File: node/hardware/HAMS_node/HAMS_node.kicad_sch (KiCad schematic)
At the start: 45 parts, among them J1 Conn_01x02, J2 Conn_02x07_Odd_Even, J3 Conn_01x04, J4 Conn_01x04, J5 Conn_01x04, J6 Conn_01x04, J7 Conn_01x08, Q1 DMP3099L, SW1 TL3305BF100QG, SW2 TL3305BF100QG, U1 STM32L031K6Tx, U2 NRF24L01_Breakout, U3 nRF24L01p SMD module, Y1 CM9V-T1A

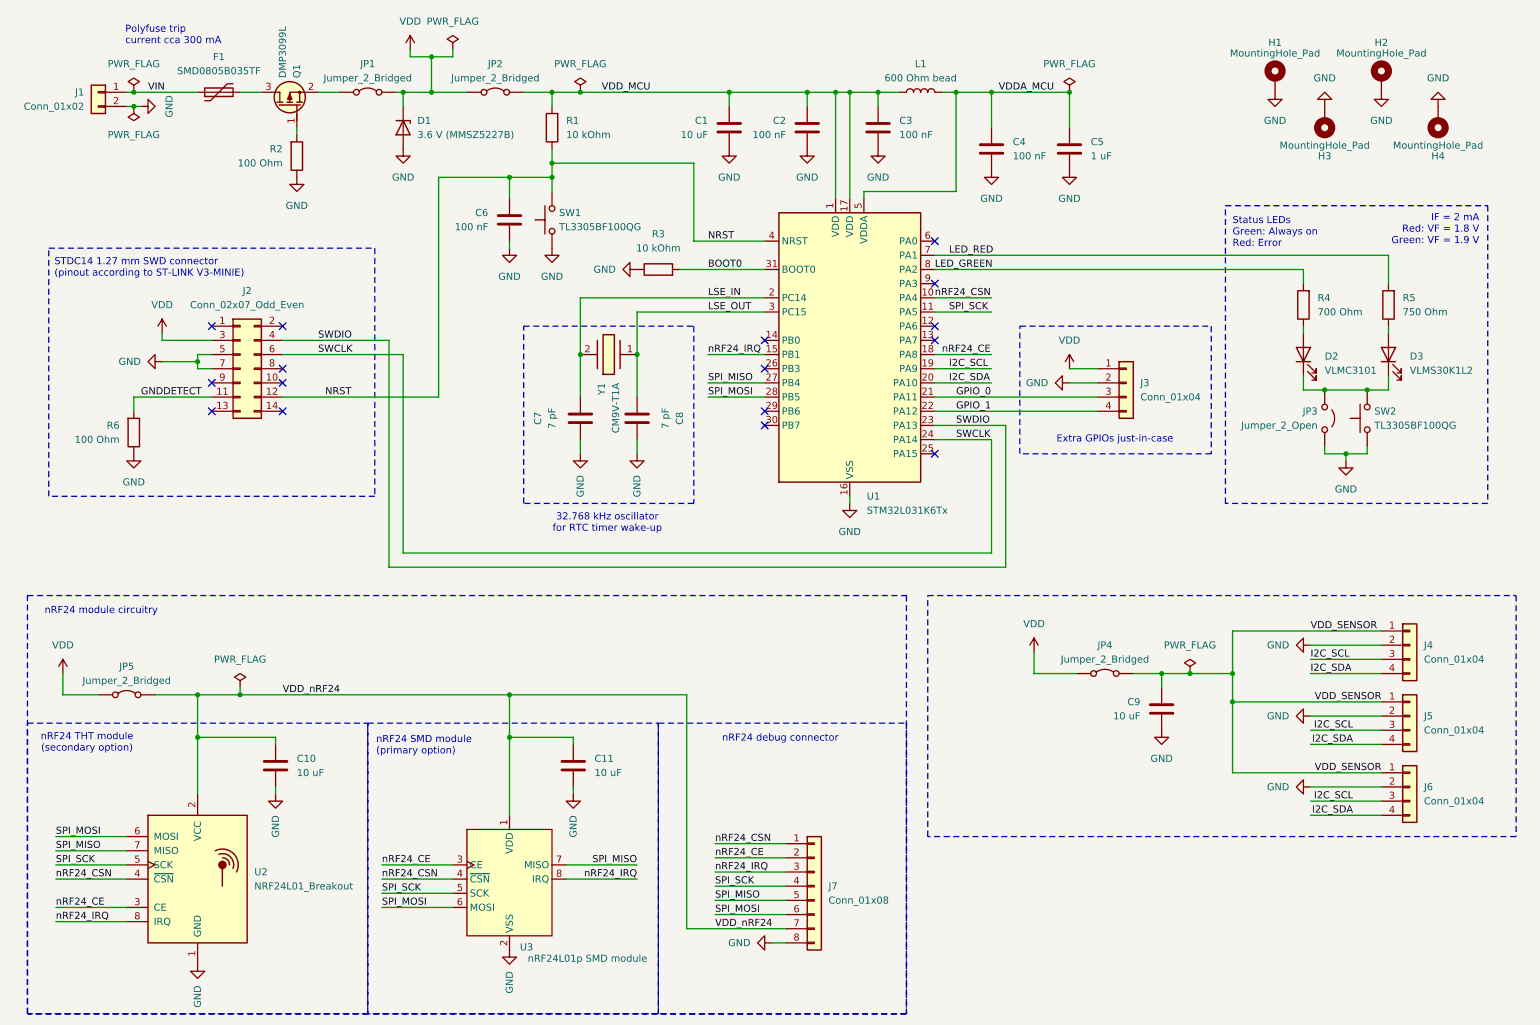
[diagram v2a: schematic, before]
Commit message: Improve HAMS node HW: PCB resize, optimization
Optimize MCU pinout with respect to PCB routing.
Change PCB size to 47.5 mm x 50 mm.
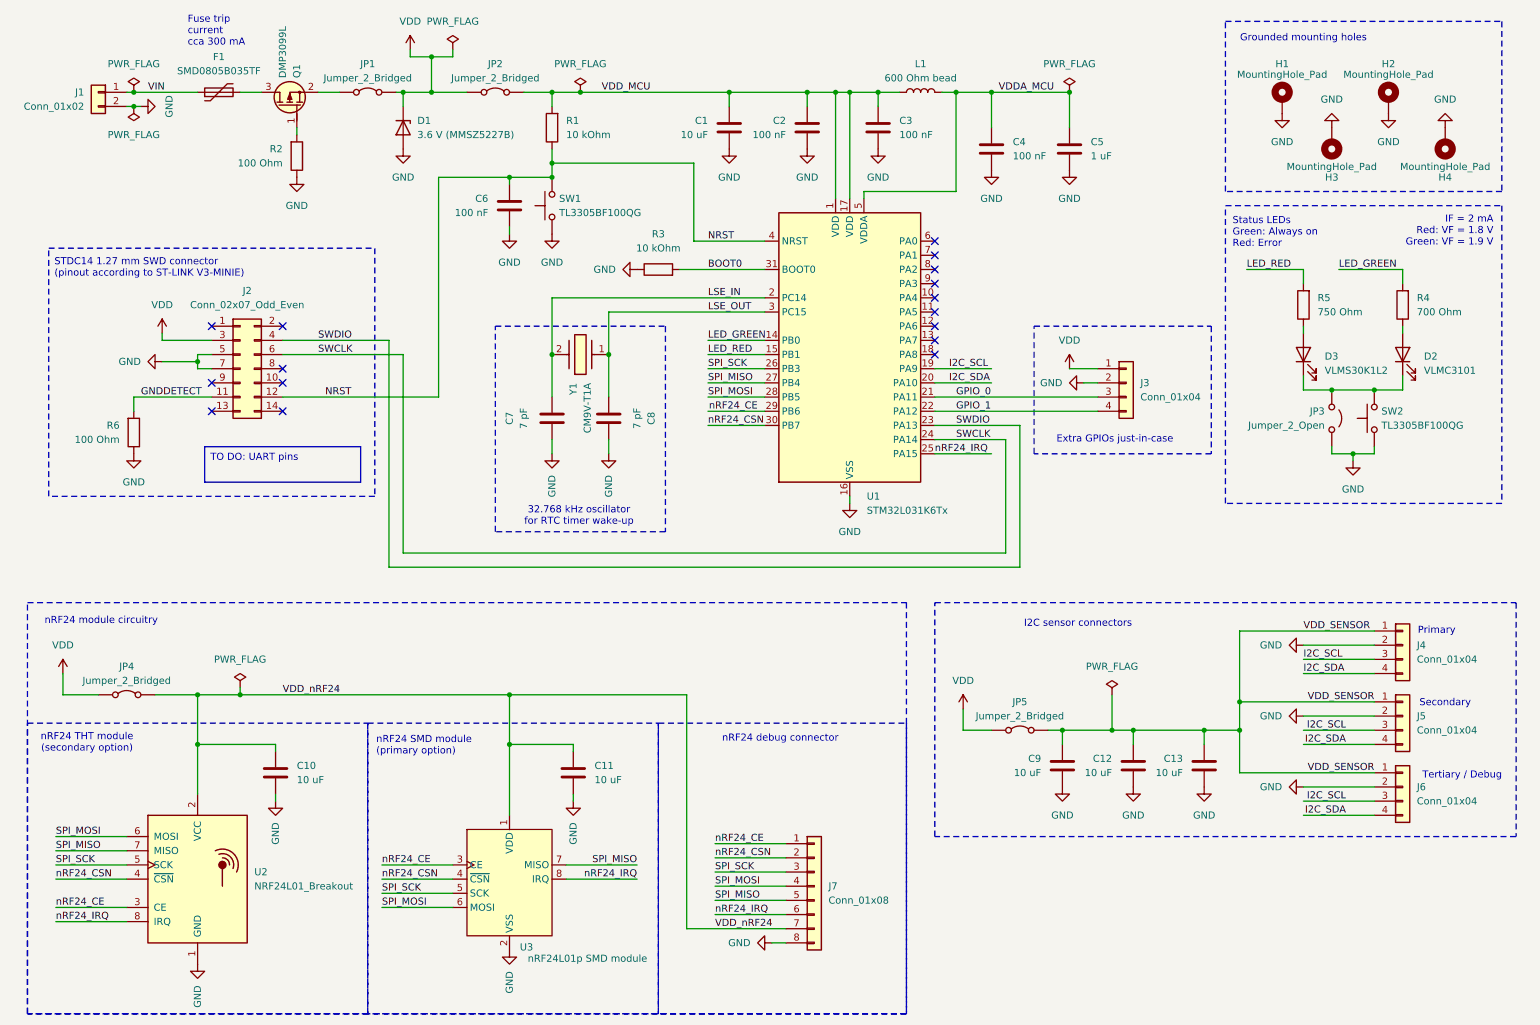
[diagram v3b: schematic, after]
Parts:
- added C12, C13: 10 uF, Capacitor_SMD:C_0603_1608Metric_Pad1.08x0.95mm_HandSolder, symbol Device:C
- J1: footprint Connector_PinSocket_2.54mm:PinSocket_1x02_P2.54mm_Horizontal -> Connector_JST:JST_XH_B2B-XH-AM_1x02_P2.50mm_Vertical
- JP1, JP2, JP3: footprint Connector_PinHeader_2.54mm:PinHeader_2x01_P2.54mm_Vertical -> Connector_PinHeader_1.27mm:PinHeader_2x01_P1.27mm_Vertical
- JP4: renamed from JP5; footprint Connector_PinHeader_2.54mm:PinHeader_2x01_P2.54mm_Vertical -> Connector_PinHeader_1.27mm:PinHeader_2x01_P1.27mm_Vertical
- JP5: renamed from JP4; footprint Connector_PinHeader_2.54mm:PinHeader_2x01_P2.54mm_Vertical -> Connector_PinHeader_1.27mm:PinHeader_2x01_P1.27mm_Vertical
- Y1: footprint PCM_Crystal_Handsoldering_AKL:Crystal_SMD_MicroCrystal_CM9V-T1A-2Pin_1.6x1.0mm_BigPads -> PCM_Crystal_AKL:Crystal_SMD_MicroCrystal_CM9V-T1A-2Pin_1.6x1.0mm_BigPads
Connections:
- net GND: now also C12.2, C13.2
- net LED_GREEN: now also U1.14 (PB0); no longer U1.8 (PA2)
- net LED_RED: now also U1.15 (PB1); no longer U1.7 (PA1)
- net SPI_MOSI: now also J7.4 (Pin_4); no longer J7.6 (Pin_6)
- net SPI_SCK: now also J7.3 (Pin_3), U1.26 (PB3); no longer J7.4 (Pin_4), U1.11 (PA5)
- net VDD_SENSOR: now also C12.1, C13.1
- net nRF24_CE: now also J7.1 (Pin_1), U1.29 (PB6); no longer J7.2 (Pin_2), U1.18 (PA8)
- net nRF24_CSN: now also J7.2 (Pin_2), U1.30 (PB7); no longer J7.1 (Pin_1), U1.10 (PA4)
- net nRF24_IRQ: now also J7.6 (Pin_6), U1.25 (PA15); no longer J7.3 (Pin_3), U1.15 (PB1)
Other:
- note added: "Fuse trip current cca 300 mA"
- note added: "Grounded mounting holes"
- note added: "I2C sensor connectors"
- note added: "Primary"
- note added: "Secondary"
- note added: "Tertiary / Debug"
- note removed: "Polyfuse trip current cca 300 mA"
- moved on the sheet: C10, C11, C6, C7, C8, C9, D2, D3, H1, H2, H3, H4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

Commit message: Improve HAMS node HW: schematic and PCB
Change LED section (compact LED, DPDT switch).
Remove VDDA ferrite bead and bulk capacitor.
Add pads for I2C pullups.
Add silkscreen labels.
Update footprints of custom symbols.
Change mounting holes to non-grounded.
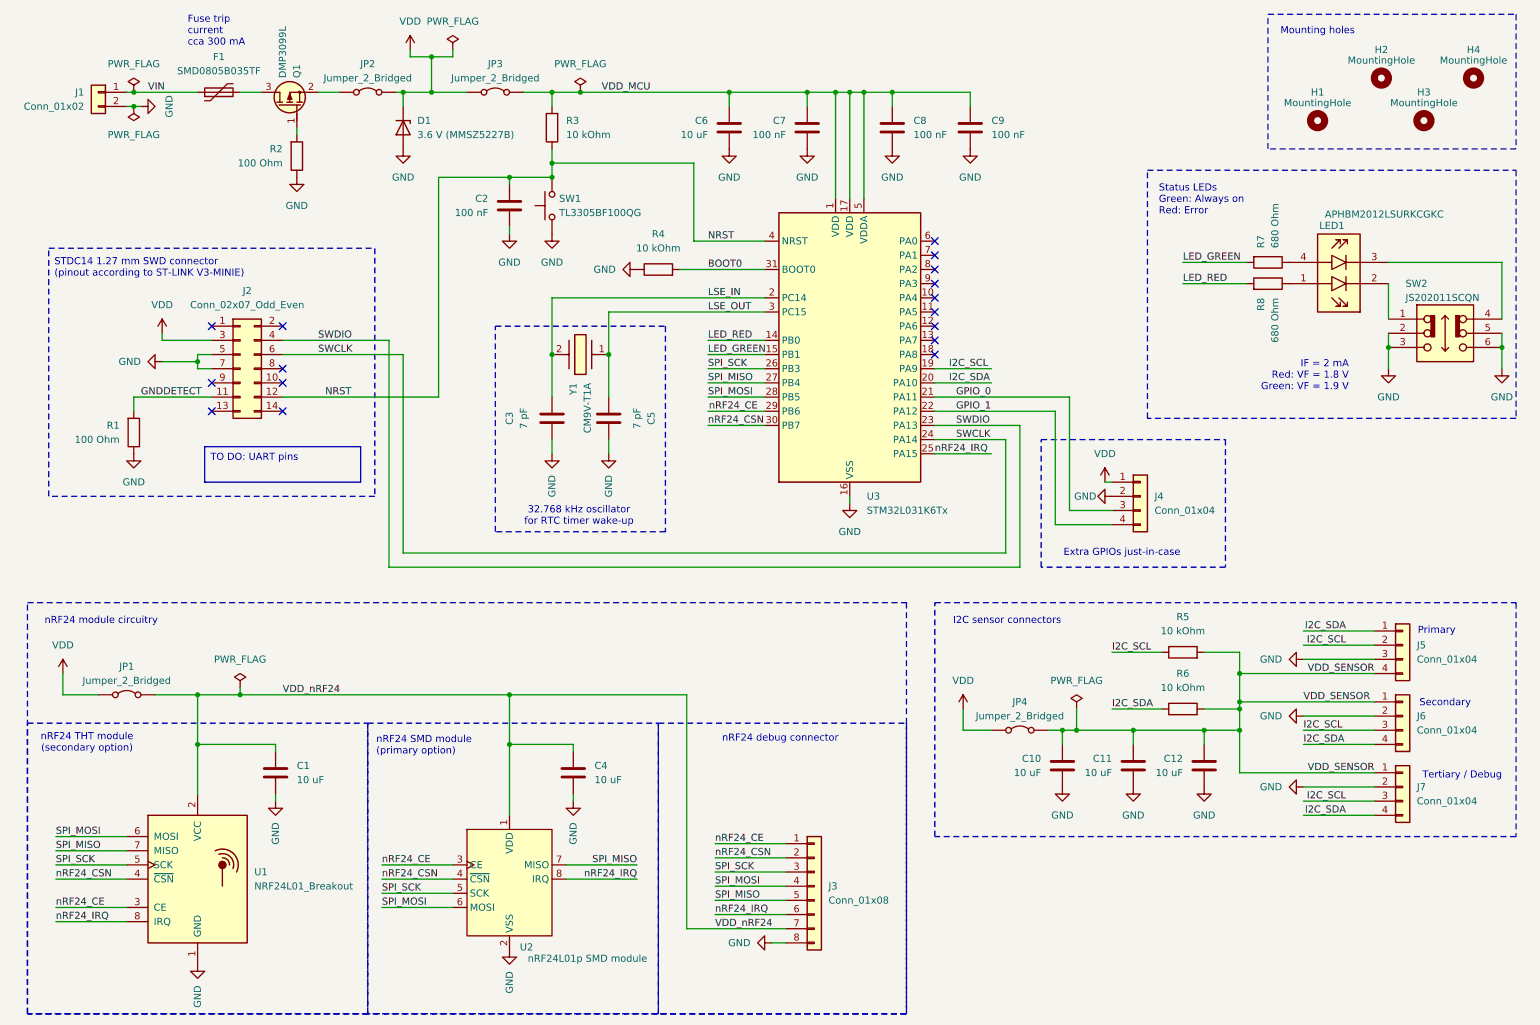
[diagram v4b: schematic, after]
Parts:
- removed C5: 1 uF, Capacitor_SMD:C_0603_1608Metric_Pad1.08x0.95mm_HandSolder, symbol Device:C
- removed D2: VLMC3101, LED_SMD:LED_PLCC-2_3.4x3.0mm_KA, symbol Device:LED
- removed D3: VLMS30K1L2, LED_SMD:LED_PLCC-2_3.4x3.0mm_KA, symbol Device:LED
- removed H1, H2, H3, H4: MountingHole_Pad, MountingHole:MountingHole_2.2mm_M2_ISO7380_Pad_TopBottom, symbol Mechanical:MountingHole_Pad
- removed JP3: Jumper_2_Open, Connector_PinHeader_1.27mm:PinHeader_2x01_P1.27mm_Vertical, symbol Jumper:Jumper_2_Open
- removed L1: 600 Ohm bead, Inductor_SMD:L_0603_1608Metric_Pad1.05x0.95mm_HandSolder, symbol Device:L
- removed SW2: TL3305BF100QG, Personal_Switches:E-Switch_TL3305BF100QG_Tactile_SPST, symbol Switch:SW_Push
- added H1, H2, H3, H4: MountingHole, MountingHole:MountingHole_2.2mm_M2_ISO7380, symbol Mechanical:MountingHole
- added LED1: APHBM2012LSURKCGKC, Personal_SamacSys:KPHBM2012QBDCGKC, symbol Personal_SamacSys:APHBM2012LSURKCGKC
- added R5, R6: 10 kOhm, Resistor_SMD:R_0603_1608Metric_Pad0.98x0.95mm_HandSolder, symbol Device:R
- added SW2: JS202011SCQN, Personal_SamacSys:JS202011SCQN, symbol Personal_SamacSys:JS202011SCQN
- R1: renamed from R6; footprint PCM_Resistor_SMD_AKL:R_0603_1608Metric_Pad1.05x0.95mm_HandSolder -> Resistor_SMD:R_0603_1608Metric_Pad0.98x0.95mm_HandSolder
- R2: footprint PCM_Resistor_SMD_AKL:R_0603_1608Metric_Pad1.05x0.95mm_HandSolder -> Resistor_SMD:R_0603_1608Metric_Pad0.98x0.95mm_HandSolder
- R3: renamed from R1; footprint PCM_Resistor_SMD_AKL:R_0603_1608Metric_Pad1.05x0.95mm_HandSolder -> Resistor_SMD:R_0603_1608Metric_Pad0.98x0.95mm_HandSolder
- R4: renamed from R3; footprint PCM_Resistor_SMD_AKL:R_0603_1608Metric_Pad1.05x0.95mm_HandSolder -> Resistor_SMD:R_0603_1608Metric_Pad0.98x0.95mm_HandSolder
- R7: renamed from R4; value 700 Ohm -> 680 Ohm; footprint PCM_Resistor_SMD_AKL:R_0603_1608Metric_Pad1.05x0.95mm_HandSolder -> Resistor_SMD:R_0603_1608Metric_Pad0.98x0.95mm_HandSolder
- R8: renamed from R5; value 750 Ohm -> 680 Ohm; footprint PCM_Resistor_SMD_AKL:R_0603_1608Metric_Pad1.05x0.95mm_HandSolder -> Resistor_SMD:R_0603_1608Metric_Pad0.98x0.95mm_HandSolder
- renumbered C10 to C1, C9 to C10, C12 to C11, C13 to C12, C6 to C2, C7 to C3, C11 to C4, C8 to C5, C1 to C6, C2 to C7, C3 to C8, C4 to C9, J7 to J3, J3 to J4, J4 to J6, J6 to J7, JP4 to JP1, JP1 to JP2, JP2 to JP3, JP5 to JP4, U2 to U1, U3 to U2, U1 to U3
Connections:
- net VDDA_MCU is gone; now on net VDD_MCU: C9.1, U3.5 (VDDA)
- net GND: now also J5.3 (Pin_3), SW2.2, SW2.3, SW2.5, SW2.6; no longer J5.2 (Pin_2)
- net I2C_SCL: now also J5.2 (Pin_2), R5.1; no longer J5.3 (Pin_3)
- net I2C_SDA: now also J5.1 (Pin_1), R6.1; no longer J5.4 (Pin_4)
- net LED_GREEN: now also U3.15 (PB1); no longer U3.14 (PB0)
- net LED_RED: now also U3.14 (PB0); no longer U3.15 (PB1)
- net VDD_SENSOR: now also J5.4 (Pin_4), R5.2, R6.2; no longer J5.1 (Pin_1)
- net at R7.1: now also LED1.4 (ANODE_GREEN)
- net at R8.1: now also LED1.1 (ANODE_RED)
- new net: LED1.2 (CATHODE_RED), SW2.1
- new net: LED1.3 (CATHODE_GREEN), SW2.4
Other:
- note added: "Mounting holes"
- note removed: "Grounded mounting holes"
- moved on the sheet: C8, C9, J4, J5, J6, R7, R8

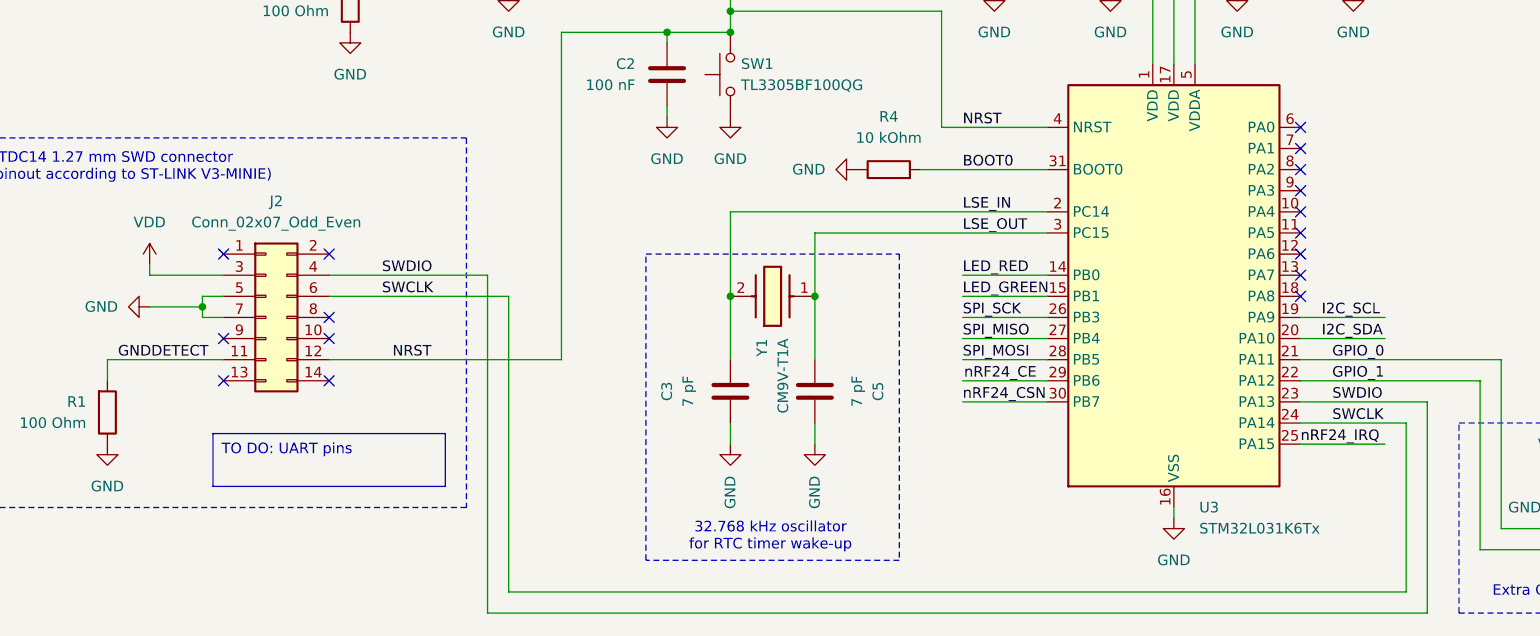
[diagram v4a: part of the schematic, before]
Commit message: Improve HAMS node HW: schematic and PCB
Add UART support to the ST-LINK programmer header.
Update task list.
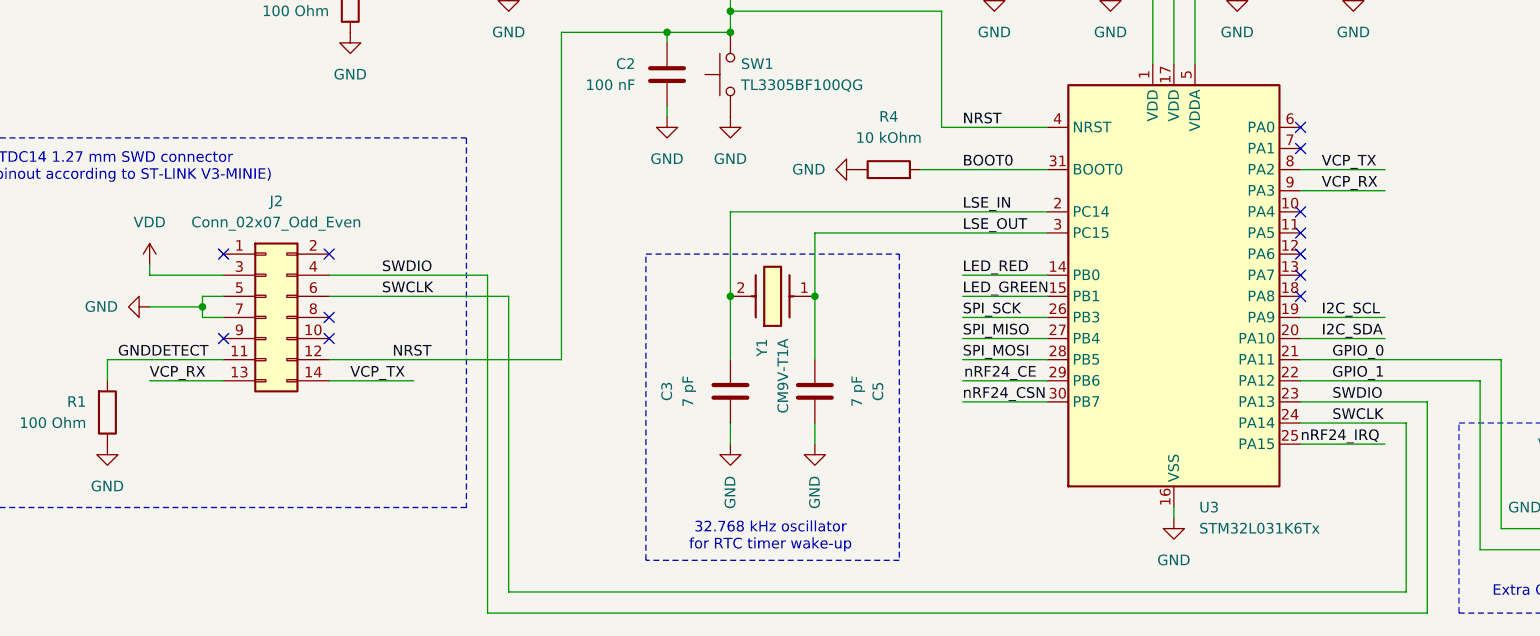
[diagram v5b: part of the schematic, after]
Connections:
- net VCP_RX: now reaches J2.13 (Pin_13)
- net VCP_RX: now also U3.9 (PA3)
- net VCP_TX: now reaches J2.14 (Pin_14)
- net VCP_TX: now also U3.8 (PA2)
- no-connect marks 16 -> 12
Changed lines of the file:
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@@
-	)
-	(no_connect
-		(at 48.26 86.36)
 	)
 	(no_connect
@@
 	)
 	(no_connect
-		(at 177.8 60.96)
-	)
-	(no_connect
 		(at 60.96 71.12)
 	)
@@
 	)
 	(no_connect
-		(at 60.96 86.36)
-	)
-	(no_connect
 		(at 60.96 81.28)
-	)
-	(no_connect
-		(at 177.8 63.5)
 	)
 	(no_connect
@@
 	(wire
 		(pts
+			(xy 39.37 86.36) (xy 48.26 86.36)
+		)
+		(stroke
+			(width 0)
+			(type default)
+		)
+	)
+	(wire
+		(pts
 			(xy 193.04 88.9) (xy 193.04 114.3)
 		)
@@
 	(wire
 		(pts
+			(xy 177.8 63.5) (xy 187.96 63.5)
+		)
+		(stroke
+			(width 0)
+			(type default)
+		)
+	)
+	(wire
+		(pts
 			(xy 82.55 111.76) (xy 190.5 111.76)
 		)
@@
 	(wire
 		(pts
+			(xy 60.96 86.36) (xy 71.12 86.36)
+		)
+		(stroke
+			(width 0)
+			(type default)
+		)
+	)
+	(wire
+		(pts
 			(xy 34.29 83.82) (xy 48.26 83.82)
 		)
@@
 		(pts
 			(xy 33.02 31.75) (xy 34.29 31.75)
+		)
+		(stroke
+			(width 0)
+			(type default)
+		)
+	)
+	(wire
+		(pts
+			(xy 177.8 60.96) (xy 187.96 60.96)
 		)
 		(stroke
@@
 		)
 	)
-	(text_box "TO DO: UART pins"
-		(exclude_from_sim no)
-		(at 46.99 92.71 0)
-		(size 27.94 6.35)
-		(stroke
-			(width 0)
-			(type default)
-		)
-		(fill
-			(type none)
-		)
-		(effects
-			(font
-				(size 1.27 1.27)
-			)
-			(justify left top)
-		)
-	)
 	(text "nRF24 THT module\n(secondary option)"
 		(exclude_from_sim no)
@@
 		)
 	)
+	(label "VCP_TX"
+		(at 180.34 60.96 0)
+		(fields_autoplaced yes)
+		(effects
+			(font
+				(size 1.27 1.27)
+			)
+			(justify left bottom)
+		)
+	)
 	(label "SPI_MISO"
 		(at 20.32 165.1 0)
@@
 		)
 	)
+	(label "VCP_RX"
+		(at 180.34 63.5 0)
+		(fields_autoplaced yes)
+		(effects
+			(font
+				(size 1.27 1.27)
+			)
+			(justify left bottom)
+		)
+	)
 	(label "I2C_SCL"
 		(at 209.55 129.54 0)
@@
 		)
 	)
+	(label "VCP_TX"
+		(at 63.5 86.36 0)
+		(fields_autoplaced yes)
+		(effects
+			(font
+				(size 1.27 1.27)
+			)
+			(justify left bottom)
+		)
+	)
 	(label "nRF24_CSN"
 		(at 20.32 170.18 0)
@@
 		(fields_autoplaced yes)
 		(effects
+			(font
+				(size 1.27 1.27)
+			)
+			(justify left bottom)
+		)
+	)
+	(label "VCP_RX"
+		(at 39.37 86.36 0)
+		(fields_autoplaced yes)
+		(effects
